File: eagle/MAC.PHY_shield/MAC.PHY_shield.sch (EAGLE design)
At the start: 21 parts, among them IC1 ENC28J60, Q1 CSM-7X-DU

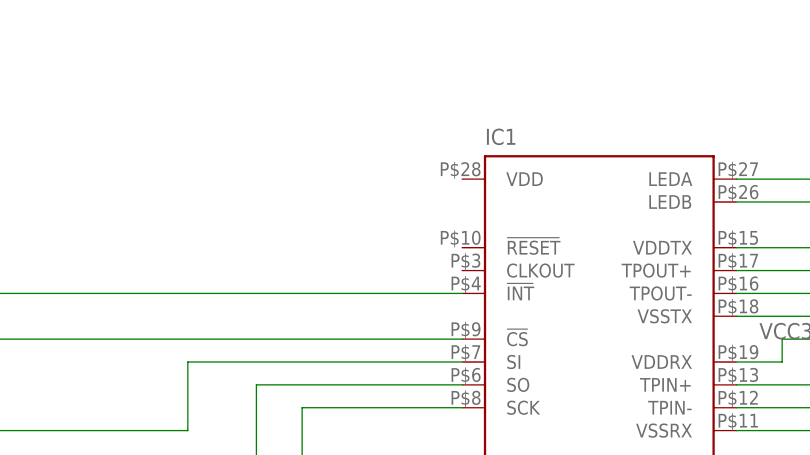
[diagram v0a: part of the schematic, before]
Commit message: Changed ENC board
Signed-off-by: Pavlo Manovi <pavlo.manovi@gmail.com>
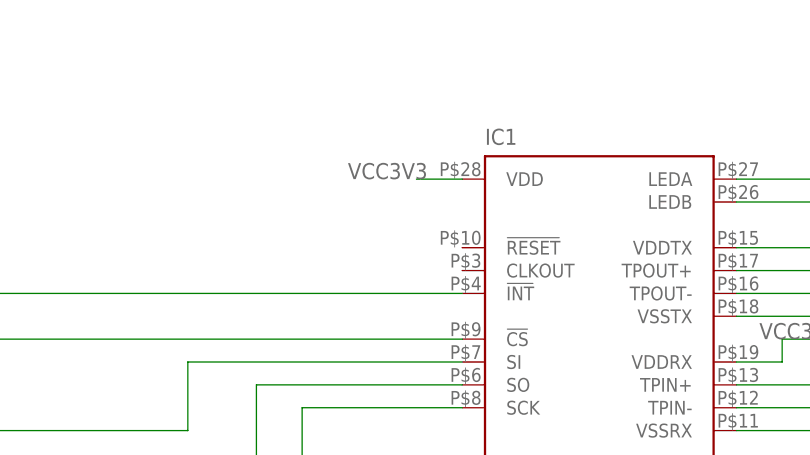
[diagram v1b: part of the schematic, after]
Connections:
- net VCC3V3: now also IC1.VDD
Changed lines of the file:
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@@
 <label x="91.44" y="17.78" size="1.778" layer="95"/>
+</segment>
+<segment>
+<pinref part="IC1" gate="G$1" pin="VDD"/>
+<wire x1="53.34" y1="68.58" x2="48.26" y2="68.58" width="0.2032" layer="91"/>
+<label x="40.64" y="68.58" size="1.778" layer="95"/>
 </segment>
 </net>

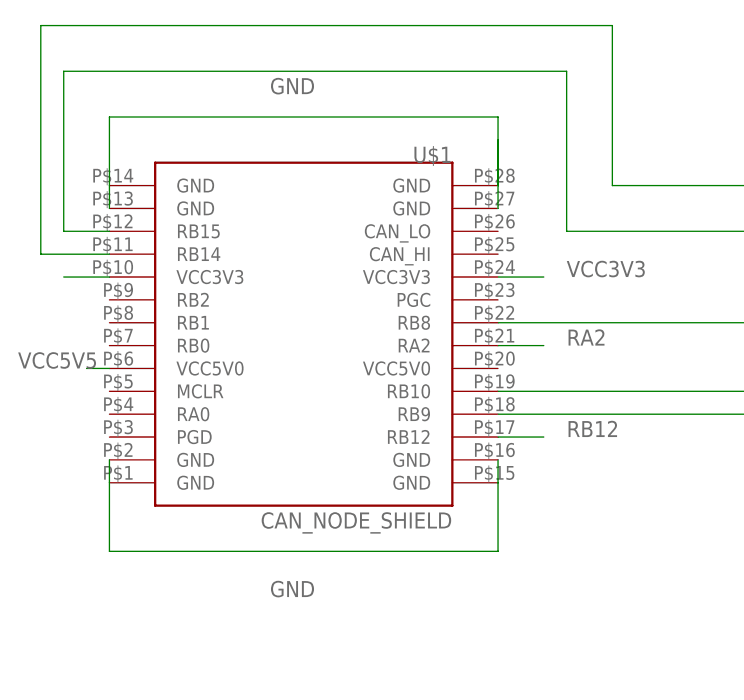
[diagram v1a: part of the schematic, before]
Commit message: Changes to bldc 4-layer. Finished ethershield v3.
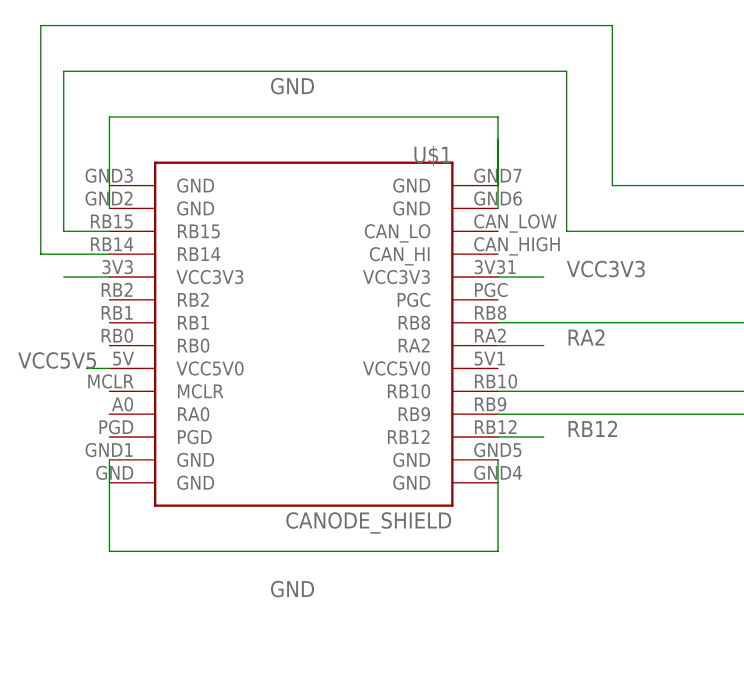
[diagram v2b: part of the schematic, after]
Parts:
- U$1: value CAN_NODE_SHIELD -> CANODE_SHIELD; device ASL:CAN_NODE_SHIELD -> ASL:CANODE_SHIELD
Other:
- moved on the sheet: U$1
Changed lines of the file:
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@@
 <?xml version="1.0" encoding="utf-8"?>
 <!DOCTYPE eagle SYSTEM "eagle.dtd">
-<eagle version="6.2">
+<eagle version="6.3">
 <drawing>
 <settings>
@@
 <layers>
 <layer number="1" name="Top" color="4" fill="1" visible="no" active="no"/>
+<layer number="2" name="Route2" color="1" fill="3" visible="no" active="no"/>
+<layer number="3" name="Route3" color="4" fill="3" visible="no" active="no"/>
+<layer number="4" name="Route4" color="1" fill="4" visible="no" active="no"/>
+<layer number="5" name="Route5" color="4" fill="4" visible="no" active="no"/>
+<layer number="6" name="Route6" color="1" fill="8" visible="no" active="no"/>
+<layer number="7" name="Route7" color="4" fill="8" visible="no" active="no"/>
+<layer number="8" name="Route8" color="1" fill="2" visible="no" active="no"/>
+<layer number="9" name="Route9" color="4" fill="2" visible="no" active="no"/>
+<layer number="10" name="Route10" color="1" fill="7" visible="no" active="no"/>
+<layer number="11" name="Route11" color="4" fill="7" visible="no" active="no"/>
+<layer number="12" name="Route12" color="1" fill="5" visible="no" active="no"/>
+<layer number="13" name="Route13" color="4" fill="5" visible="no" active="no"/>
+<layer number="14" name="Route14" color="1" fill="6" visible="no" active="no"/>
+<layer number="15" name="Route15" color="4" fill="6" visible="no" active="no"/>
 <layer number="16" name="Bottom" color="1" fill="1" visible="no" active="no"/>
 <layer number="17" name="Pads" color="2" fill="1" visible="no" active="no"/>
@@
 <part name="Q1" library="crystal" deviceset="CSM-7X-DU" device=""/>
 <part name="GND1" library="ASL" deviceset="GND" device=""/>
-<part name="U$1" library="ASL" deviceset="CAN_NODE_SHIELD" device=""/>
+<part name="U$1" library="ASL" deviceset="CANODE_SHIELD" device=""/>
 <part name="IC1" library="ASL" deviceset="ENC28J60" device=""/>
 <part name="U$3" library="ASL" deviceset="MAGJACK" device=""/>

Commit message: Polished up MAC-PHY Board.
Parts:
- renumbered U$4 to F1
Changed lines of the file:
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@@
 <?xml version="1.0" encoding="utf-8"?>
 <!DOCTYPE eagle SYSTEM "eagle.dtd">
-<eagle version="6.1">
+<eagle version="6.4">
 <drawing>
 <settings>
@@
 <part name="R6" library="ASL" deviceset="RESISTOR" device="0805-RES" value="49.9"/>
 <part name="R7" library="ASL" deviceset="RESISTOR" device="0805-RES" value="49.9"/>
-<part name="U$4" library="ASL" deviceset="FERRITE_BEAD" device=""/>
+<part name="F1" library="ASL" deviceset="FERRITE_BEAD" device=""/>
 <part name="C3" library="ASL" deviceset="CAP" device="1206" value=".1 uF"/>
 <part name="C4" library="ASL" deviceset="CAP" device="1206" value=".1 uF"/>
@@
 <instance part="R6" gate="G$1" x="177.8" y="30.48" rot="R270"/>
 <instance part="R7" gate="G$1" x="177.8" y="20.32" rot="R270"/>
-<instance part="U$4" gate="G$1" x="215.9" y="71.12"/>
+<instance part="F1" gate="G$1" x="215.9" y="71.12"/>
 <instance part="C3" gate="G$1" x="215.9" y="58.42"/>
 <instance part="C4" gate="G$1" x="190.5" y="25.4"/>
@@
 <wire x1="208.28" y1="53.34" x2="177.8" y2="53.34" width="0.2032" layer="91"/>
 <junction x="177.8" y="53.34"/>
-<pinref part="U$4" gate="G$1" pin="2"/>
+<pinref part="F1" gate="G$1" pin="2"/>
 <junction x="215.9" y="63.5"/>
 <pinref part="C3" gate="G$1" pin="1"/>
@@
 </segment>
 <segment>
-<pinref part="U$4" gate="G$1" pin="1"/>
+<pinref part="F1" gate="G$1" pin="1"/>
 <wire x1="215.9" y1="78.74" x2="215.9" y2="81.28" width="0.2032" layer="91"/>
 <label x="215.9" y="83.82" size="1.778" layer="95"/>
